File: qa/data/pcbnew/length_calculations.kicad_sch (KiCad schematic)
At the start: 12 parts

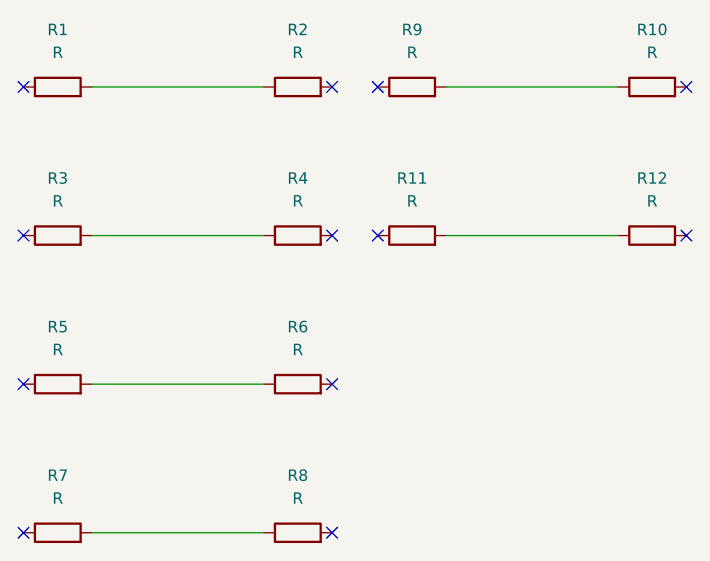
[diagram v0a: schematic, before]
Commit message: Improve via height electrial length calculations
For vias which terminate electrically in an internal layer, only
count half of that internal layer height. This means a subsequent
via on the same route will not result on the internal layer being
double-counted.

Fixes https://gitlab.com/kicad/code/kicad/-/work_items/24118
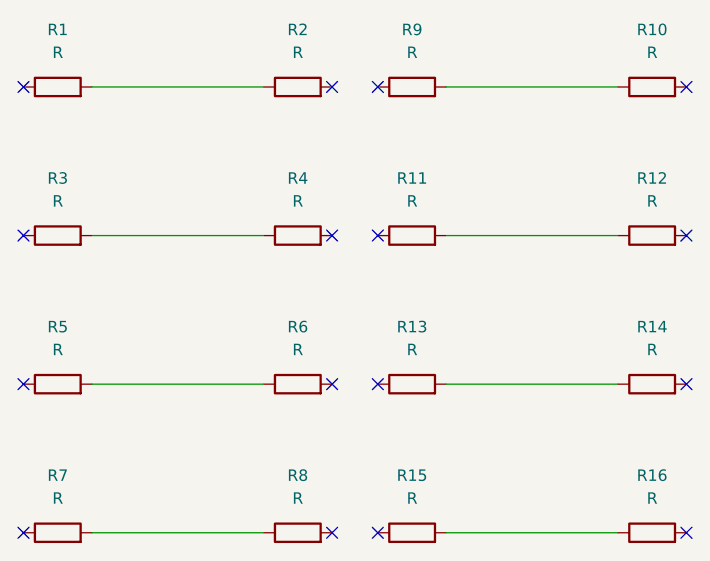
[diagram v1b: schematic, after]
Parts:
- added R13, R14, R15, R16: R, Resistor_SMD:R_0805_2012Metric, symbol Device:R
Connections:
- new net: R13.2, R14.1
- new net: R15.2, R16.1
- no-connect marks 12 -> 16
